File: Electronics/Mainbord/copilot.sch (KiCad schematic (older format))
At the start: 24 parts, among them J33 Screw_Terminal_01x10, J34 Screw_Terminal_01x10, J35 Screw_Terminal_01x10, U45 74HC165, U46 74HC165, U47 74HC165, U48 74HC165

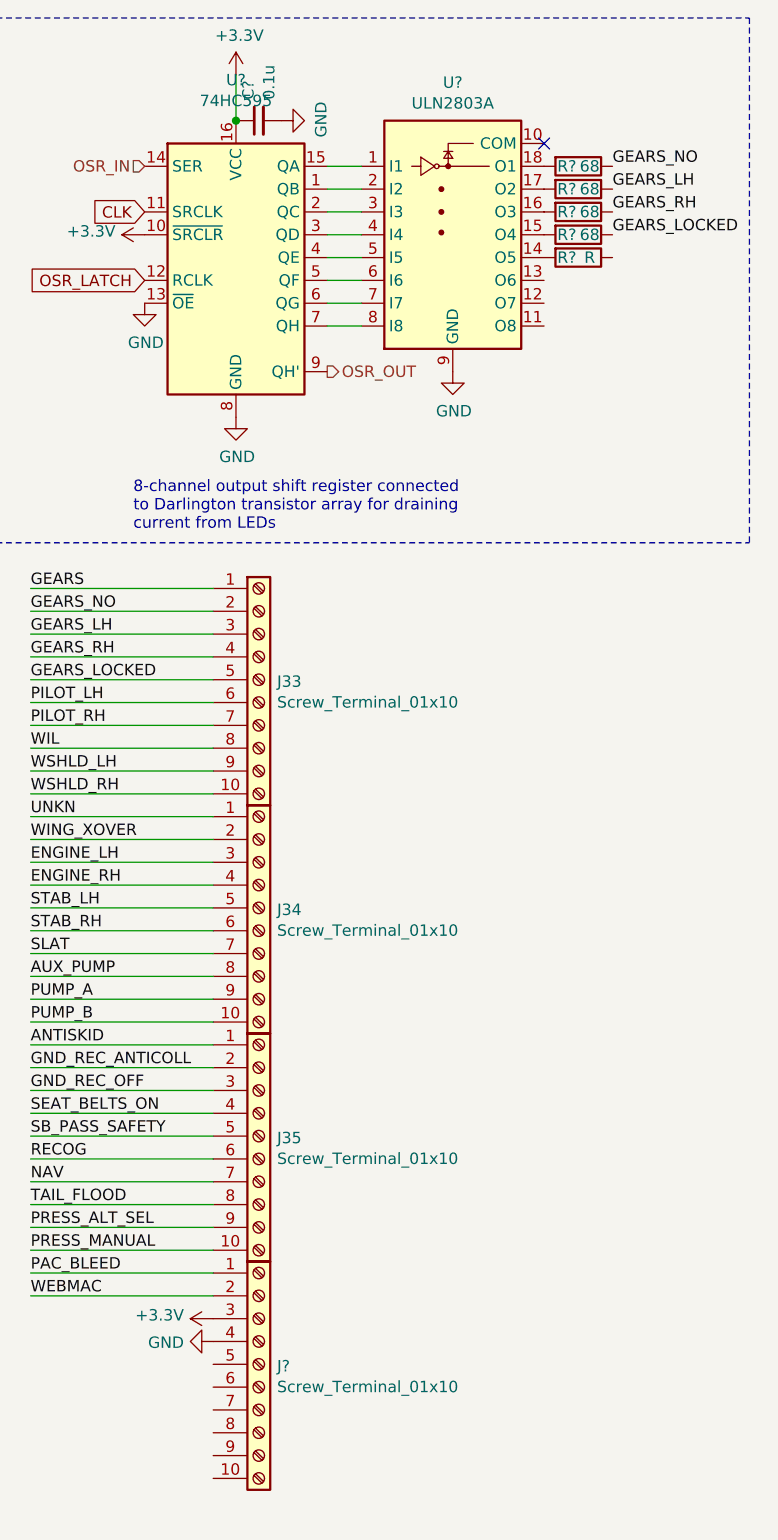
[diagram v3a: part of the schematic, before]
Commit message: Electronics - Adds LCSC part numbers and footprints
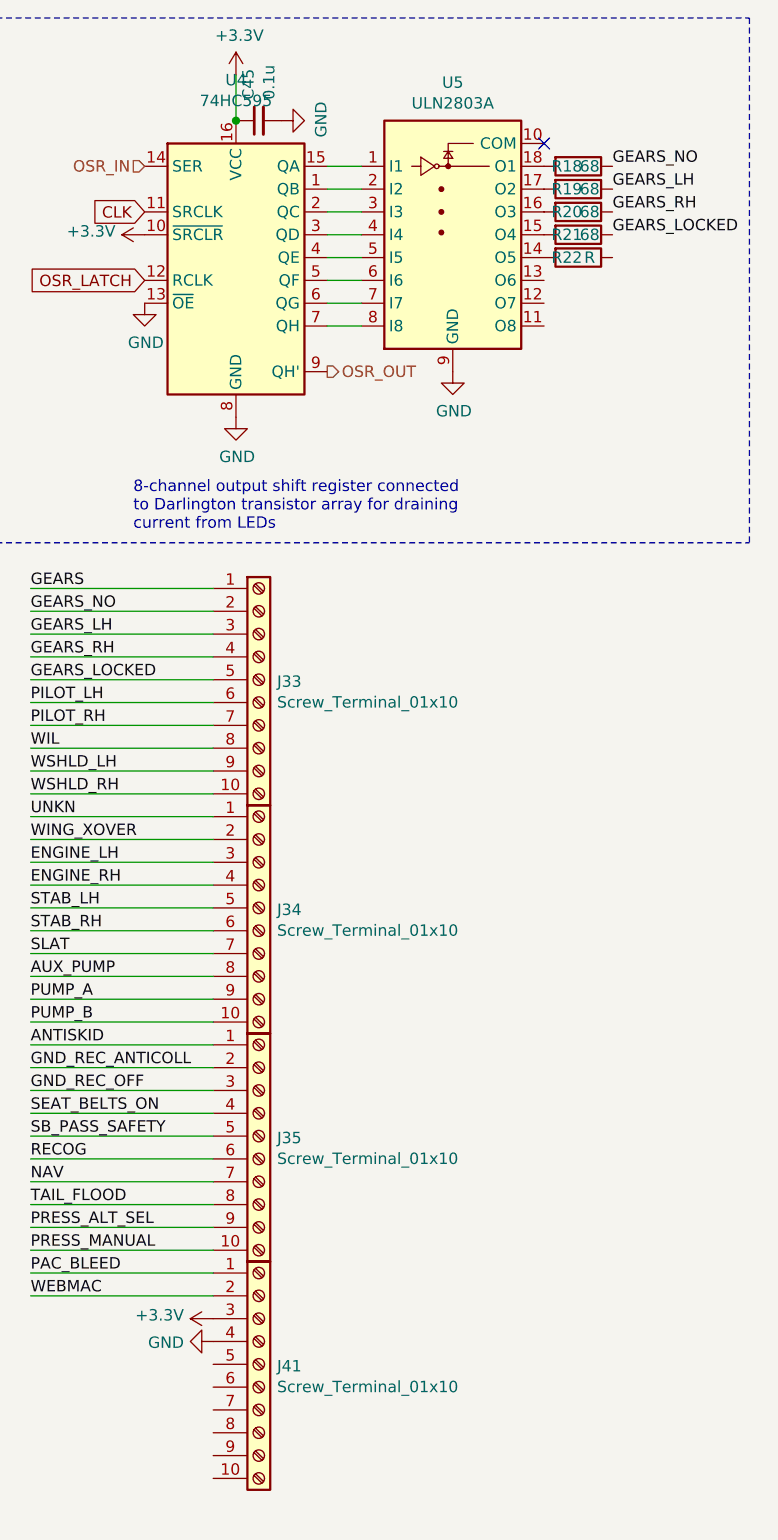
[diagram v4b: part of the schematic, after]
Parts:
- U4: renamed from U?; footprint (none) -> Package_SO:SOIC-16_3.9x9.9mm_P1.27mm; LCSC (none) -> C5947
- U45, U46, U47, U48: footprint (none) -> Package_SO:SOIC-16_3.9x9.9mm_P1.27mm; LCSC (none) -> C5613
- U5: renamed from U?; footprint (none) -> Package_SO:SOIC-18W_7.5x11.6mm_P1.27mm; LCSC (none) -> C9683
- gave numbers to parts that had none: 7
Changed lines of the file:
@@
 F 0 "U45" H 3100 2847 60  0000 C CNN
 F 1 "74HC165" H 3100 2741 60  0000 C CNN
-F 2 "" H 5290 730 60  0001 C CNN
+F 2 "Package_SO:SOIC-16_3.9x9.9mm_P1.27mm" H 5290 730 60  0001 C CNN
 F 3 "" H 5290 730 60  0001 C CNN
+F 4 "C5613" H 3100 1950 50  0001 C CNN "LCSC"
 	1    3100 1950
 	1    0    0    -1
@@
 F 0 "U46" H 3100 4547 60  0000 C CNN
 F 1 "74HC165" H 3100 4441 60  0000 C CNN
-F 2 "" H 5290 2430 60  0001 C CNN
+F 2 "Package_SO:SOIC-16_3.9x9.9mm_P1.27mm" H 5290 2430 60  0001 C CNN
 F 3 "" H 5290 2430 60  0001 C CNN
+F 4 "C5613" H 3100 3650 50  0001 C CNN "LCSC"
 	1    3100 3650
 	1    0    0    -1
@@
 F 0 "U47" H 3100 6247 60  0000 C CNN
 F 1 "74HC165" H 3100 6141 60  0000 C CNN
-F 2 "" H 5290 4130 60  0001 C CNN
+F 2 "Package_SO:SOIC-16_3.9x9.9mm_P1.27mm" H 5290 4130 60  0001 C CNN
 F 3 "" H 5290 4130 60  0001 C CNN
+F 4 "C5613" H 3100 5350 50  0001 C CNN "LCSC"
 	1    3100 5350
 	1    0    0    -1
@@
 F 0 "U48" H 3100 7947 60  0000 C CNN
 F 1 "74HC165" H 3100 7841 60  0000 C CNN
-F 2 "" H 5290 5830 60  0001 C CNN
+F 2 "Package_SO:SOIC-16_3.9x9.9mm_P1.27mm" H 5290 5830 60  0001 C CNN
 F 3 "" H 5290 5830 60  0001 C CNN
+F 4 "C5613" H 3100 7050 50  0001 C CNN "LCSC"
 	1    3100 7050
 	1    0    0    -1
@@
 AR Path="/5DC174D4/5E02571A" Ref="C?"  Part="1"
 AR Path="/5DC31399/5E02571A" Ref="C?"  Part="1"
-AR Path="/5DC2EEA6/5E02571A" Ref="C?"  Part="1"
-F 0 "C?" H 5742 1246 50  0000 L CNN
+AR Path="/5DC2EEA6/5E02571A" Ref="C45"  Part="1"
+F 0 "C45" H 5742 1246 50  0000 L CNN
 F 1 "0.1u" H 5742 1155 50  0000 L CNN
 F 2 "" H 5650 1200 50  0001 C CNN
@@
 AR Path="/5DC174D4/5E025721" Ref="#PWR?"  Part="1"
 AR Path="/5DC31399/5E025721" Ref="#PWR?"  Part="1"
-AR Path="/5DC2EEA6/5E025721" Ref="#PWR?"  Part="1"
-F 0 "#PWR?" H 5750 950 50  0001 C CNN
+AR Path="/5DC2EEA6/5E025721" Ref="#PWR0271"  Part="1"
+F 0 "#PWR0271" H 5750 950 50  0001 C CNN
 F 1 "GND" H 5755 1027 50  0000 C CNN
 F 2 "" H 5750 1200 50  0001 C CNN
@@
 AR Path="/5DC174D4/5E025728" Ref="U?"  Part="1"
 AR Path="/5DC31399/5E025728" Ref="U?"  Part="1"
-AR Path="/5DC2EEA6/5E025728" Ref="U?"  Part="1"
-F 0 "U?" H 5550 2578 50  0000 C CNN
+AR Path="/5DC2EEA6/5E025728" Ref="U4"  Part="1"
+F 0 "U4" H 5550 2578 50  0000 C CNN
 F 1 "74HC595" H 5550 2487 50  0000 C CNN
-F 2 "" H 5550 1800 50  0001 C CNN
+F 2 "Package_SO:SOIC-16_3.9x9.9mm_P1.27mm" H 5550 1800 50  0001 C CNN
 F 3 "http://www.ti.com/lit/ds/symlink/sn74hc595.pdf" H 5550 1800 50  0001 C CNN
+F 4 "C5947" H 5550 1800 50  0001 C CNN "LCSC"
 	1    5550 1800
 	1    0    0    -1
@@
 AR Path="/5DC174D4/5E025730" Ref="#PWR?"  Part="1"
 AR Path="/5DC31399/5E025730" Ref="#PWR?"  Part="1"
-AR Path="/5DC2EEA6/5E025730" Ref="#PWR?"  Part="1"
-F 0 "#PWR?" H 5550 2250 50  0001 C CNN
+AR Path="/5DC2EEA6/5E025730" Ref="#PWR0272"  Part="1"
+F 0 "#PWR0272" H 5550 2250 50  0001 C CNN
 F 1 "GND" H 5555 2327 50  0000 C CNN
 F 2 "" H 5550 2500 50  0001 C CNN
@@
 AR Path="/5DC174D4/5E025737" Ref="#PWR?"  Part="1"
 AR Path="/5DC31399/5E025737" Ref="#PWR?"  Part="1"
-AR Path="/5DC2EEA6/5E025737" Ref="#PWR?"  Part="1"
-F 0 "#PWR?" H 5150 1750 50  0001 C CNN
+AR Path="/5DC2EEA6/5E025737" Ref="#PWR0273"  Part="1"
+F 0 "#PWR0273" H 5150 1750 50  0001 C CNN
 F 1 "GND" H 5155 1827 50  0000 C CNN
 F 2 "" H 5150 2000 50  0001 C CNN
@@
 AR Path="/5DC174D4/5E02573E" Ref="#PWR?"  Part="1"
 AR Path="/5DC31399/5E02573E" Ref="#PWR?"  Part="1"
-AR Path="/5DC2EEA6/5E02573E" Ref="#PWR?"  Part="1"
-F 0 "#PWR?" H 5550 850 50  0001 C CNN
+AR Path="/5DC2EEA6/5E02573E" Ref="#PWR0274"  Part="1"
+F 0 "#PWR0274" H 5550 850 50  0001 C CNN
 F 1 "+3.3V" H 5565 1173 50  0000 C CNN
 F 2 "" H 5550 1000 50  0001 C CNN
@@
 AR Path="/5DC174D4/5E025744" Ref="#PWR?"  Part="1"
 AR Path="/5DC31399/5E025744" Ref="#PWR?"  Part="1"
-AR Path="/5DC2EEA6/5E025744" Ref="#PWR?"  Part="1"
-F 0 "#PWR?" H 5150 1550 50  0001 C CNN
+AR Path="/5DC2EEA6/5E025744" Ref="#PWR0275"  Part="1"
+F 0 "#PWR0275" H 5150 1550 50  0001 C CNN
 F 1 "+3.3V" V 5165 1828 50  0000 L CNN
 F 2 "" H 5150 1700 50  0001 C CNN
@@
 AR Path="/5DC31399/5E025752" Ref="U?"  Part="1"
 AR Path="/5DC174D4/5E025752" Ref="U?"  Part="1"
-AR Path="/5DC2EEA6/5E025752" Ref="U?"  Part="1"
-F 0 "U?" H 6500 2167 50  0000 C CNN
+AR Path="/5DC2EEA6/5E025752" Ref="U5"  Part="1"
+F 0 "U5" H 6500 2167 50  0000 C CNN
 F 1 "ULN2803A" H 6500 2076 50  0000 C CNN
-F 2 "" H 6550 950 50  0001 L CNN
+F 2 "Package_SO:SOIC-18W_7.5x11.6mm_P1.27mm" H 6550 950 50  0001 L CNN
 F 3 "http://www.ti.com/lit/ds/symlink/uln2803a.pdf" H 6600 1400 50  0001 C CNN
+F 4 "C9683" H 6500 1600 50  0001 C CNN "LCSC"
 	1    6500 1600
 	1    0    0    -1
@@
 AR Path="/5DC174D4/5E025759" Ref="#PWR?"  Part="1"
 AR Path="/5DC31399/5E025759" Ref="#PWR?"  Part="1"
-AR Path="/5DC2EEA6/5E025759" Ref="#PWR?"  Part="1"
-F 0 "#PWR?" H 6500 2050 50  0001 C CNN
+AR Path="/5DC2EEA6/5E025759" Ref="#PWR0276"  Part="1"
+F 0 "#PWR0276" H 6500 2050 50  0001 C CNN
 F 1 "GND" H 6505 2127 50  0000 C CNN
 F 2 "" H 6500 2300 50  0001 C CNN
@@
 AR Path="/5DC31399/5E02575F" Ref="R?"  Part="1"
 AR Path="/5DC174D4/5E02575F" Ref="R?"  Part="1"
-AR Path="/5DC2EEA6/5E02575F" Ref="R?"  Part="1"
-F 0 "R?" V 7050 1350 50  0000 C CNN
+AR Path="/5DC2EEA6/5E02575F" Ref="R18"  Part="1"
+F 0 "R18" V 7050 1350 50  0000 C CNN
 F 1 "68" V 7050 1450 50  0000 C CNN
 F 2 "" V 6980 1400 50  0001 C CNN
@@
 AR Path="/5DC31399/5E025766" Ref="R?"  Part="1"
 AR Path="/5DC174D4/5E025766" Ref="R?"  Part="1"
-AR Path="/5DC2EEA6/5E025766" Ref="R?"  Part="1"
-F 0 "R?" V 7050 1450 50  0000 C CNN
+AR Path="/5DC2EEA6/5E025766" Ref="R19"  Part="1"
+F 0 "R19" V 7050 1450 50  0000 C CNN
 F 1 "68" V 7050 1550 50  0000 C CNN
 F 2 "" V 6980 1500 50  0001 C CNN
@@
 AR Path="/5DC31399/5E02576D" Ref="R?"  Part="1"
 AR Path="/5DC174D4/5E02576D" Ref="R?"  Part="1"
-AR Path="/5DC2EEA6/5E02576D" Ref="R?"  Part="1"
-F 0 "R?" V 7050 1550 50  0000 C CNN
+AR Path="/5DC2EEA6/5E02576D" Ref="R20"  Part="1"
+F 0 "R20" V 7050 1550 50  0000 C CNN
 F 1 "68" V 7050 1650 50  0000 C CNN
 F 2 "" V 6980 1600 50  0001 C CNN
@@
 AR Path="/5DC31399/5E025774" Ref="R?"  Part="1"
 AR Path="/5DC174D4/5E025774" Ref="R?"  Part="1"
-AR Path="/5DC2EEA6/5E025774" Ref="R?"  Part="1"
-F 0 "R?" V 7050 1650 50  0000 C CNN
+AR Path="/5DC2EEA6/5E025774" Ref="R21"  Part="1"
+F 0 "R21" V 7050 1650 50  0000 C CNN
 F 1 "68" V 7050 1750 50  0000 C CNN
 F 2 "" V 6980 1700 50  0001 C CNN
@@
 AR Path="/5DC31399/5E02577B" Ref="R?"  Part="1"
 AR Path="/5DC174D4/5E02577B" Ref="R?"  Part="1"
-AR Path="/5DC2EEA6/5E02577B" Ref="R?"  Part="1"
-F 0 "R?" V 7050 1750 50  0000 C CNN
+AR Path="/5DC2EEA6/5E02577B" Ref="R22"  Part="1"
+F 0 "R22" V 7050 1750 50  0000 C CNN
 F 1 "R" V 7050 1850 50  0000 C CNN
 F 2 "" V 6980 1800 50  0001 C CNN
@@
 P 5650 6650
 AR Path="/5DB5DCD1/5E051D92" Ref="J?"  Part="1"
-AR Path="/5DC2EEA6/5E051D92" Ref="J?"  Part="1"
-F 0 "J?" H 5730 6642 50  0000 L CNN
+AR Path="/5DC2EEA6/5E051D92" Ref="J41"  Part="1"
+F 0 "J41" H 5730 6642 50  0000 L CNN
 F 1 "Screw_Terminal_01x10" H 5730 6551 50  0000 L CNN
 F 2 "" H 5650 6650 50  0001 C CNN
@@
 P 5450 6450
 AR Path="/5DB5DCD1/5E056D0F" Ref="#PWR?"  Part="1"
-AR Path="/5DC2EEA6/5E056D0F" Ref="#PWR?"  Part="1"
-F 0 "#PWR?" H 5450 6300 50  0001 C CNN
+AR Path="/5DC2EEA6/5E056D0F" Ref="#PWR0277"  Part="1"
+F 0 "#PWR0277" H 5450 6300 50  0001 C CNN
 F 1 "+3.3V" V 5465 6578 50  0000 L CNN
 F 2 "" H 5450 6450 50  0001 C CNN
@@
 P 5450 6550
 AR Path="/5DB5DCD1/5E056D7A" Ref="#PWR?"  Part="1"
-AR Path="/5DC2EEA6/5E056D7A" Ref="#PWR?"  Part="1"
-F 0 "#PWR?" H 5450 6300 50  0001 C CNN
+AR Path="/5DC2EEA6/5E056D7A" Ref="#PWR0278"  Part="1"
+F 0 "#PWR0278" H 5450 6300 50  0001 C CNN
 F 1 "GND" V 5455 6422 50  0000 R CNN
 F 2 "" H 5450 6550 50  0001 C CNN
